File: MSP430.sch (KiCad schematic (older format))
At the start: 30 parts, among them P1 CONN_02X07, P3 CONN_01X06, SW1 2M1-SP1-T2-B4-M6RE, U12 SN74AUP1G06DCKR, U13 SN74AUP1G06DCKR, U6 MSP430F2274TRHAR

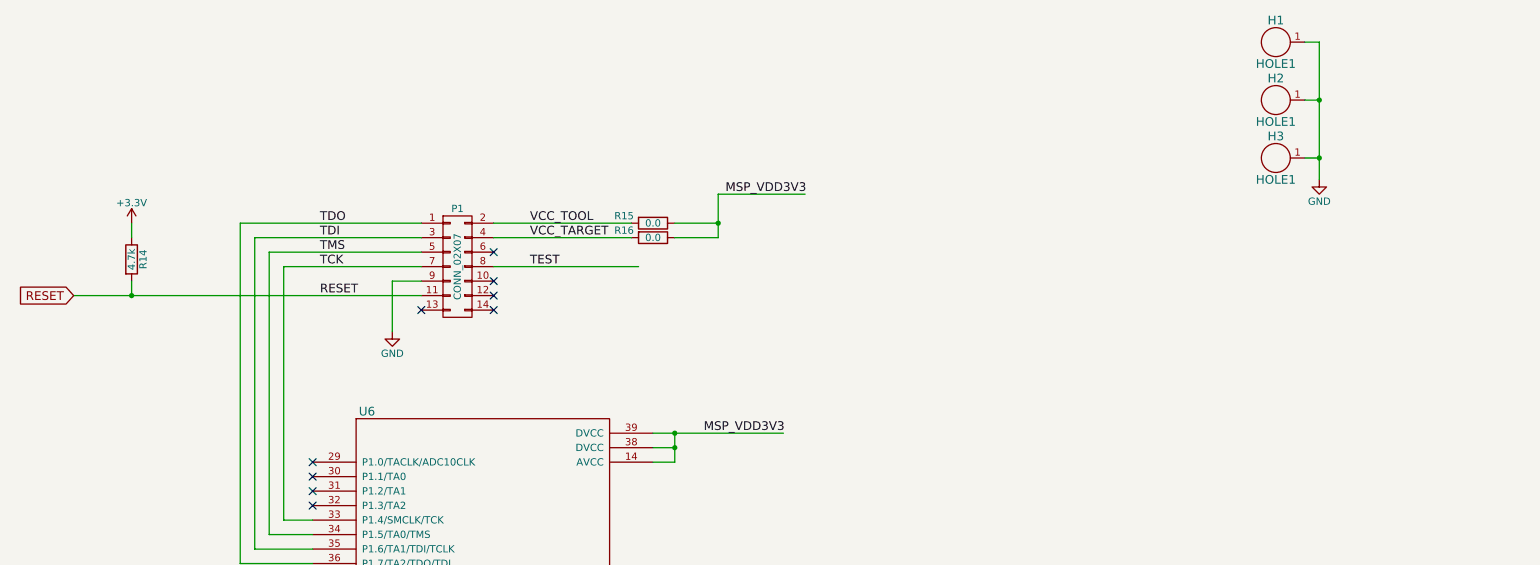
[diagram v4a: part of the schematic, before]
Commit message: Schematic Titles
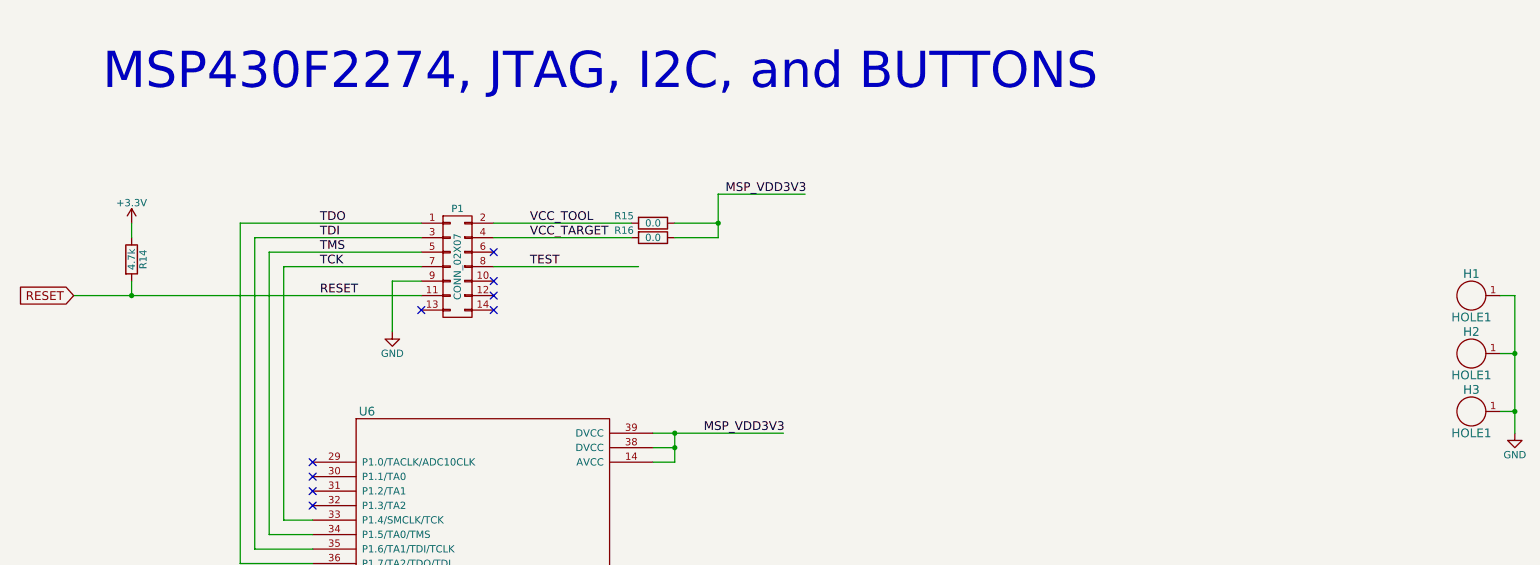
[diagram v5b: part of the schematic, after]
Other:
- note added: "MSP430F2274, JTAG, I2C, and BUTTONS"
- moved on the sheet: H1, H2, H3
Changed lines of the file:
@@
 L HOLE1 H1
 U 1 1 56F98079
-P 12650 1000
-F 0 "H1" H 12650 1150 60  0000 C CNN
-F 1 "HOLE1" H 12650 850 60  0000 C CNN
-F 2 "Mounting_Holes:MountingHole_4.3mm_M4_Pad" H 12650 1000 60  0001 C CNN
-F 3 "" H 12650 1000 60  0000 C CNN
-	1    12650 1000
+P 14000 2750
+F 0 "H1" H 14000 2900 60  0000 C CNN
+F 1 "HOLE1" H 14000 2600 60  0000 C CNN
+F 2 "Mounting_Holes:MountingHole_4.3mm_M4_Pad" H 14000 2750 60  0001 C CNN
+F 3 "" H 14000 2750 60  0000 C CNN
+	1    14000 2750
 	1    0    0    -1
 $EndComp
@@
 L HOLE1 H2
 U 1 1 56F9810C
-P 12650 1400
-F 0 "H2" H 12650 1550 60  0000 C CNN
-F 1 "HOLE1" H 12650 1250 60  0000 C CNN
-F 2 "Mounting_Holes:MountingHole_4.3mm_M4_Pad" H 12650 1400 60  0001 C CNN
-F 3 "" H 12650 1400 60  0000 C CNN
-	1    12650 1400
+P 14000 3150
+F 0 "H2" H 14000 3300 60  0000 C CNN
+F 1 "HOLE1" H 14000 3000 60  0000 C CNN
+F 2 "Mounting_Holes:MountingHole_4.3mm_M4_Pad" H 14000 3150 60  0001 C CNN
+F 3 "" H 14000 3150 60  0000 C CNN
+	1    14000 3150
 	1    0    0    -1
 $EndComp
@@
 L HOLE1 H3
 U 1 1 56F9815A
-P 12650 1800
-F 0 "H3" H 12650 1950 60  0000 C CNN
-F 1 "HOLE1" H 12650 1650 60  0000 C CNN
-F 2 "Mounting_Holes:MountingHole_4.3mm_M4_Pad" H 12650 1800 60  0001 C CNN
-F 3 "" H 12650 1800 60  0000 C CNN
-	1    12650 1800
+P 14000 3550
+F 0 "H3" H 14000 3700 60  0000 C CNN
+F 1 "HOLE1" H 14000 3400 60  0000 C CNN
+F 2 "Mounting_Holes:MountingHole_4.3mm_M4_Pad" H 14000 3550 60  0001 C CNN
+F 3 "" H 14000 3550 60  0000 C CNN
+	1    14000 3550
 	1    0    0    -1
 $EndComp
@@
 L GND #PWR050
 U 1 1 56F98389
-P 12950 1950
-F 0 "#PWR050" H 12950 1700 50  0001 C CNN
-F 1 "GND" H 12950 1800 50  0000 C CNN
-F 2 "" H 12950 1950 60  0000 C CNN
-F 3 "" H 12950 1950 60  0000 C CNN
-	1    12950 1950
+P 14300 3700
+F 0 "#PWR050" H 14300 3450 50  0001 C CNN
+F 1 "GND" H 14300 3550 50  0000 C CNN
+F 2 "" H 14300 3700 60  0000 C CNN
+F 3 "" H 14300 3700 60  0000 C CNN
+	1    14300 3700
 	1    0    0    -1
 $EndComp
@@
 Connection ~ 12550 8150
 Wire Wire Line
-	12850 1000 12950 1000
-Wire Wire Line
-	12950 1000 12950 1950
-Wire Wire Line
-	12950 1800 12850 1800
-Wire Wire Line
-	12850 1400 12950 1400
-Connection ~ 12950 1400
-Connection ~ 12950 1800
+	14200 2750 14300 2750
+Wire Wire Line
+	14300 2750 14300 3700
+Wire Wire Line
+	14300 3550 14200 3550
+Wire Wire Line
+	14200 3150 14300 3150
+Connection ~ 14300 3150
+Connection ~ 14300 3550
 Wire Wire Line
 	12550 8700 12550 8600
@@
 	5300 6950 5300 8150
 NoConn ~ 8350 4950
+Text Notes 4550 1350 0    250  ~ 0
+MSP430F2274, JTAG, I2C, and BUTTONS
 $EndSCHEMATC

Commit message: Changed BOM for several components
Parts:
- U6: Cost (none) -> 6.48; Link (none) -> http://www.mouser.com/ProductDetail/Texas-Instruments/MSP43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; Part # (none) -> MSP430F2274TRHAT; Supplier (none) -> Mouser
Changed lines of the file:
@@
 F 2 "Housings_DFN_QFN:QFN-40-1EP_6x6mm_Pitch0.5mm" H 6300 3600 60  0001 C CNN
 F 3 "" H 6300 3600 60  0000 C CNN
+F 4 "MSP430F2274TRHAT" H 6300 3600 60  0001 C CNN "Part #"
+F 5 "6.48" H 6300 3600 60  0001 C CNN "Cost"
+F 6 "http://www.mouser.com/ProductDetail/Texas-Instruments/MSP430F2274TRHAT/?qs=sGAEpiMZZMsp%252bcahb6g%252bW2X2XUDb8dT1L0nI2hcddmM%3d" H 6300 3600 60  0001 C CNN "Link"
+F 7 "Mouser" H 6300 3600 60  0001 C CNN "Supplier"
 	1    6300 3600
 	1    0    0    -1
